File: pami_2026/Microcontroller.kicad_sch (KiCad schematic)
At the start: 1 part, among them U1 ESP32-WROOM-E

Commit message: WIP actuators
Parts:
- added C9: C, symbol Device:C
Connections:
- net +3.3V: now also C9.1; no longer U1.2 (3V3)
- net GND: now also U1.39 (GND_THERMAL)
- net SW_Team: now reaches U1.10 (DAC_1/ADC2_CH8/GPIO25)
- net SERVO_1: now reaches U1.11 (DAC_2/ADC2_CH9/GPIO26)
- net SERVO_2: now reaches U1.12 (ADC2_CH7/GPIO27)
- net PWM_B: now reaches U1.27 (GPIO16)
- net DC_A1: now reaches U1.28 (GPIO17)
- net PWM_A: now reaches U1.29 (GPIO5)
- net DC_A2: now reaches U1.30 (GPIO18)
- net DC_B1: now reaches U1.31 (GPIO19)
- net DC_B2: now reaches U1.33 (GPIO21)
- net TEAM_RGB: now reaches U1.36 (GPIO22)
- net SW_Tirette: now reaches U1.37 (GPIO23)
- new net: C9.2, U1.2 (3V3)

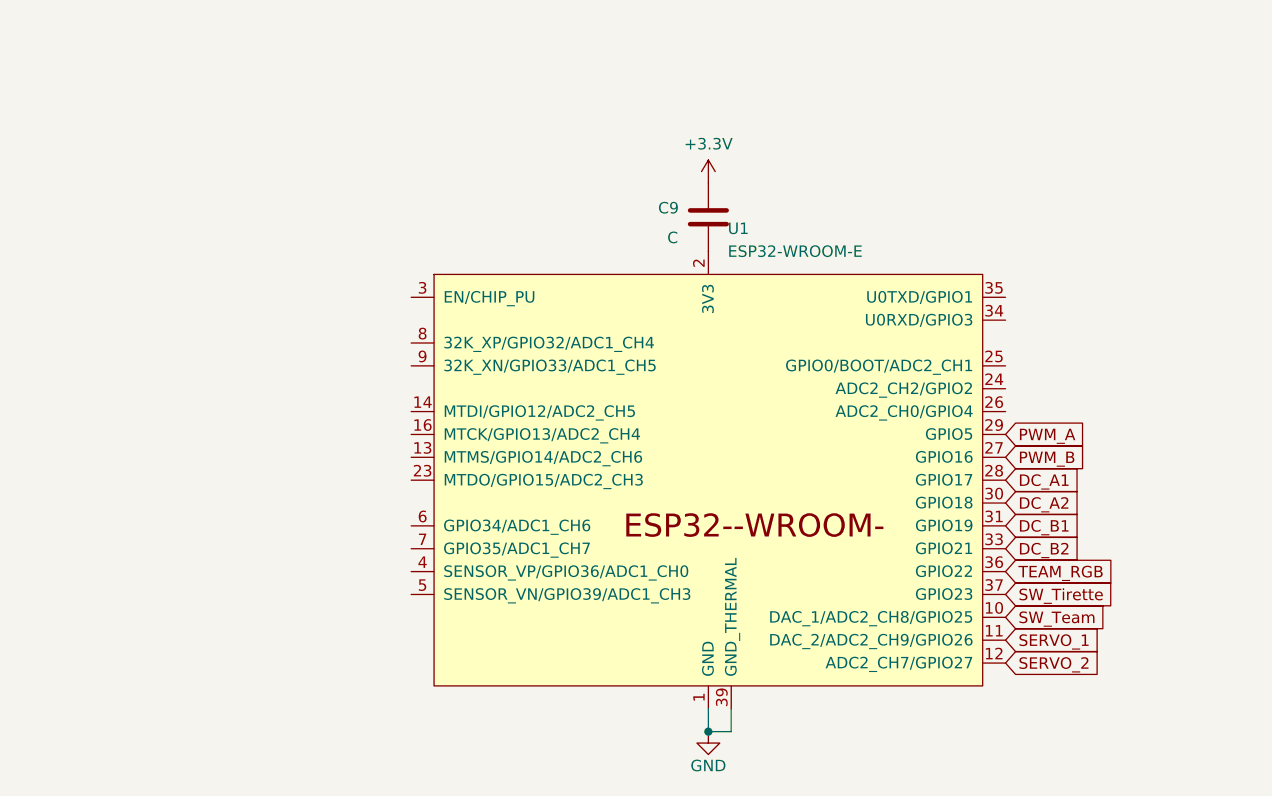
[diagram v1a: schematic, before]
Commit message: WIP USB programmer
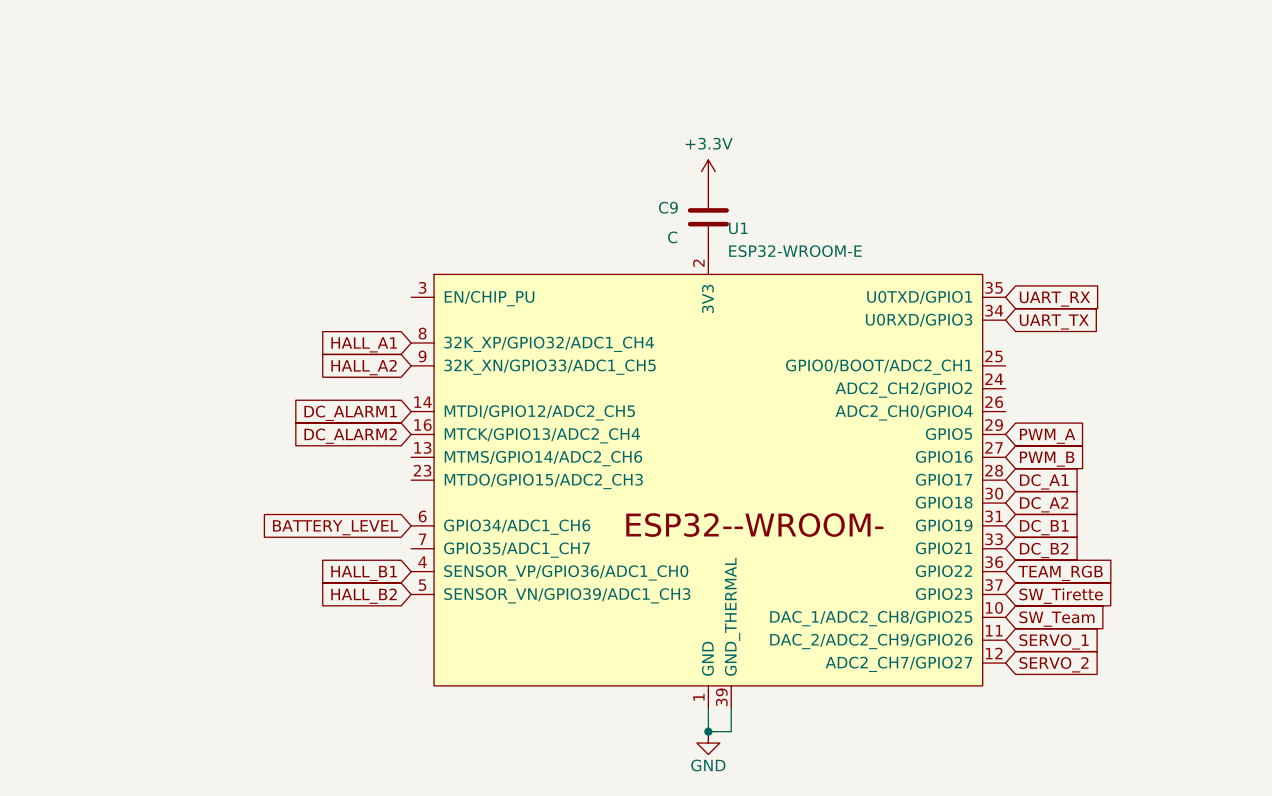
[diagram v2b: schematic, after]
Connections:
- net DC_ALARM1: now reaches U1.14 (MTDI/GPIO12/ADC2_CH5)
- net DC_ALARM2: now reaches U1.16 (MTCK/GPIO13/ADC2_CH4)
- net UART_TX: now reaches U1.34 (U0RXD/GPIO3)
- net UART_RX: now reaches U1.35 (U0TXD/GPIO1)
- net HALL_B1: now reaches U1.4 (SENSOR_VP/GPIO36/ADC1_CH0)
- net HALL_B2: now reaches U1.5 (SENSOR_VN/GPIO39/ADC1_CH3)
- net BATTERY_LEVEL: now reaches U1.6 (GPIO34/ADC1_CH6)
- net HALL_A1: now reaches U1.8 (32K_XP/GPIO32/ADC1_CH4)
- net HALL_A2: now reaches U1.9 (32K_XN/GPIO33/ADC1_CH5)
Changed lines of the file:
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@@
+		)
+	)
+	(global_label "UART_RX"
+		(shape input)
+		(at 176.53 63.5 0)
+		(fields_autoplaced yes)
+		(effects
+			(font
+				(size 1.27 1.27)
+			)
+			(justify left)
+		)
+		(property "Intersheetrefs" "${INTERSHEET_REFS}"
+			(at 187.619 63.5 0)
+			(effects
+				(font
+					(size 1.27 1.27)
+				)
+				(justify left)
+				(hide yes)
+			)
 		)
 	)
@@
 		)
 	)
+	(global_label "HALL_A2"
+		(shape input)
+		(at 110.49 71.12 180)
+		(fields_autoplaced yes)
+		(effects
+			(font
+				(size 1.27 1.27)
+			)
+			(justify right)
+		)
+		(property "Intersheetrefs" "${INTERSHEET_REFS}"
+			(at 99.7638 71.12 0)
+			(effects
+				(font
+					(size 1.27 1.27)
+				)
+				(justify right)
+				(hide yes)
+			)
+		)
+	)
 	(global_label "SW_Team"
 		(shape input)
@@
 		)
 	)
+	(global_label "BATTERY_LEVEL"
+		(shape input)
+		(at 110.49 88.9 180)
+		(fields_autoplaced yes)
+		(effects
+			(font
+				(size 1.27 1.27)
+			)
+			(justify right)
+		)
+		(property "Intersheetrefs" "${INTERSHEET_REFS}"
+			(at 93.293 88.9 0)
+			(effects
+				(font
+					(size 1.27 1.27)
+				)
+				(justify right)
+				(hide yes)
+			)
+		)
+	)
+	(global_label "DC_ALARM1"
+		(shape input)
+		(at 110.49 76.2 180)
+		(fields_autoplaced yes)
+		(effects
+			(font
+				(size 1.27 1.27)
+			)
+			(justify right)
+		)
+		(property "Intersheetrefs" "${INTERSHEET_REFS}"
+			(at 96.861 76.2 0)
+			(effects
+				(font
+					(size 1.27 1.27)
+				)
+				(justify right)
+				(hide yes)
+			)
+		)
+	)
 	(global_label "PWM_B"
 		(shape input)
@@
 		)
 	)
+	(global_label "HALL_B2"
+		(shape input)
+		(at 110.49 96.52 180)
+		(fields_autoplaced yes)
+		(effects
+			(font
+				(size 1.27 1.27)
+			)
+			(justify right)
+		)
+		(property "Intersheetrefs" "${INTERSHEET_REFS}"
+			(at 99.5824 96.52 0)
+			(effects
+				(font
+					(size 1.27 1.27)
+				)
+				(justify right)
+				(hide yes)
+			)
+		)
+	)
 	(global_label "PWM_A"
 		(shape input)
@@
 		)
 	)
+	(global_label "UART_TX"
+		(shape input)
+		(at 176.53 66.04 0)
+		(fields_autoplaced yes)
+		(effects
+			(font
+				(size 1.27 1.27)
+			)
+			(justify left)
+		)
+		(property "Intersheetrefs" "${INTERSHEET_REFS}"
+			(at 187.3166 66.04 0)
+			(effects
+				(font
+					(size 1.27 1.27)
+				)
+				(justify left)
+				(hide yes)
+			)
+		)
+	)
+	(global_label "HALL_A1"
+		(shape input)
+		(at 110.49 68.58 180)
+		(fields_autoplaced yes)
+		(effects
+			(font
+				(size 1.27 1.27)
+			)
+			(justify right)
+		)
+		(property "Intersheetrefs" "${INTERSHEET_REFS}"
+			(at 99.7638 68.58 0)
+			(effects
+				(font
+					(size 1.27 1.27)
+				)
+				(justify right)
+				(hide yes)
+			)
+		)
+	)
 	(global_label "SW_Tirette"
 		(shape input)
@@
 				(hide yes)
 			)
+		)
+	)
+	(global_label "DC_ALARM2"
+		(shape input)
+		(at 110.49 78.74 180)
+		(fields_autoplaced yes)
+		(effects
+			(font
+				(size 1.27 1.27)
+			)
+			(justify right)
+		)
+		(property "Intersheetrefs" "${INTERSHEET_REFS}"
+			(at 96.861 78.74 0)
+			(effects
+				(font
+					(size 1.27 1.27)
+				)
+				(justify right)
+				(hide yes)
+			)
+		)
+	)
+	(global_label "HALL_B1"
+		(shape input)
+		(at 110.49 93.98 180)
+		(fields_autoplaced yes)
+		(effects
+			(font
+				(size 1.27 1.27)
+			)
+			(justify right)
+		)
+		(property "Intersheetrefs" "${INTERSHEET_REFS}"
+			(at 99.5824 93.98 0)
+			(effects
+				(font
+					(size 1.27 1.27)
+				)
+				(justify right)
+				(hide yes)
+			)

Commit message: Change DC drivers, apply datasheet recommendations, add big capacitor, remove USB programmer for simple connector
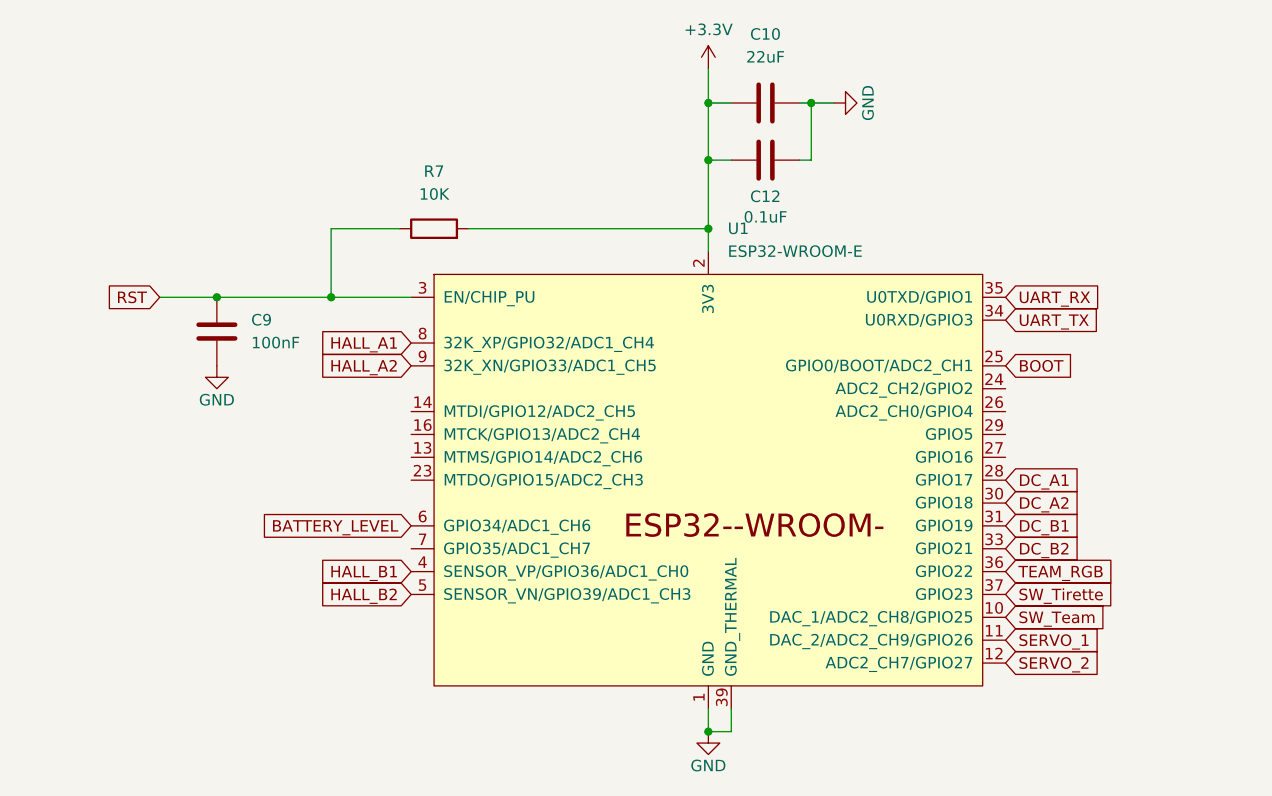
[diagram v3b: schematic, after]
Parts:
- added C10: 22uF, symbol Device:C
- added C12: 0.1uF, symbol Device:C
- added R7: 10K, symbol Device:R
- C9: value C -> 100nF
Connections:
- net +3.3V: now also U1.2 (3V3), C10.1, C12.1, R7.2; no longer C9.1
- net GND: now also C9.2, C10.2, C12.2
- net BOOT: now reaches U1.25 (GPIO0/BOOT/ADC2_CH1)
- net RST: now reaches U1.3 (EN/CHIP_PU)
- net RST: now also C9.1, R7.1
- net DC_ALARM1: no longer names the net of U1.14 (MTDI/GPIO12/ADC2_CH5)
- net DC_ALARM2: no longer names the net of U1.16 (MTCK/GPIO13/ADC2_CH4)
- net PWM_A: no longer names the net of U1.29 (GPIO5)
- net PWM_B: no longer names the net of U1.27 (GPIO16)

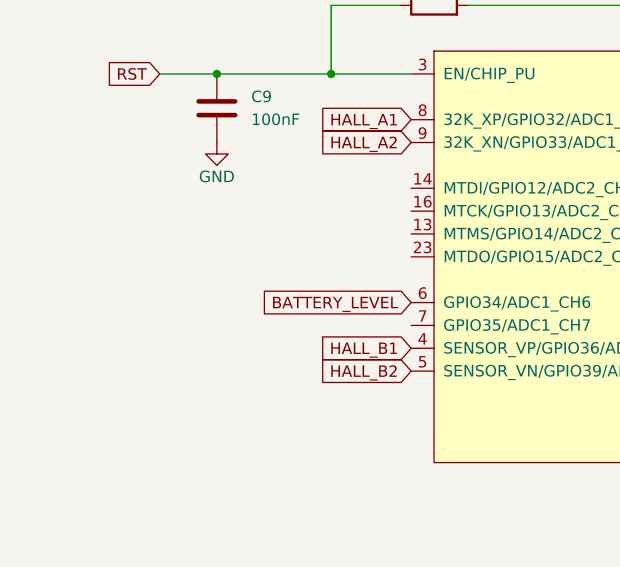
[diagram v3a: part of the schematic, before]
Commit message: Hall pull up
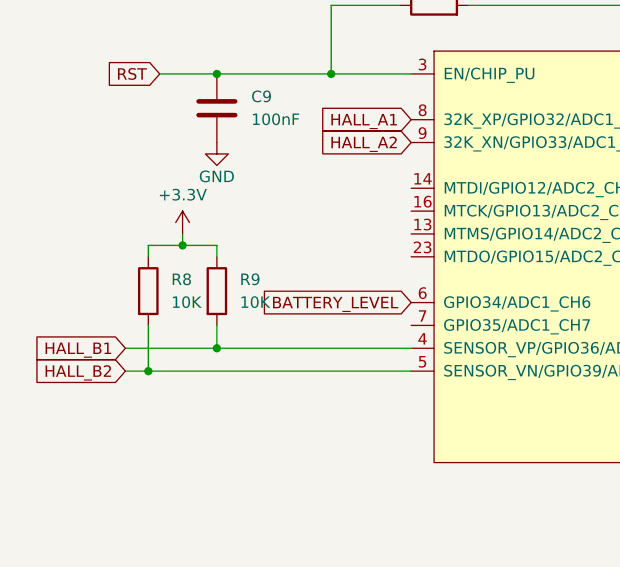
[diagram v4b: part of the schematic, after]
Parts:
- added R8, R9: 10K, symbol Device:R
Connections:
- net +3.3V: now also R8.1, R9.1
- net HALL_B1: now also R9.2
- net HALL_B2: now also R8.2

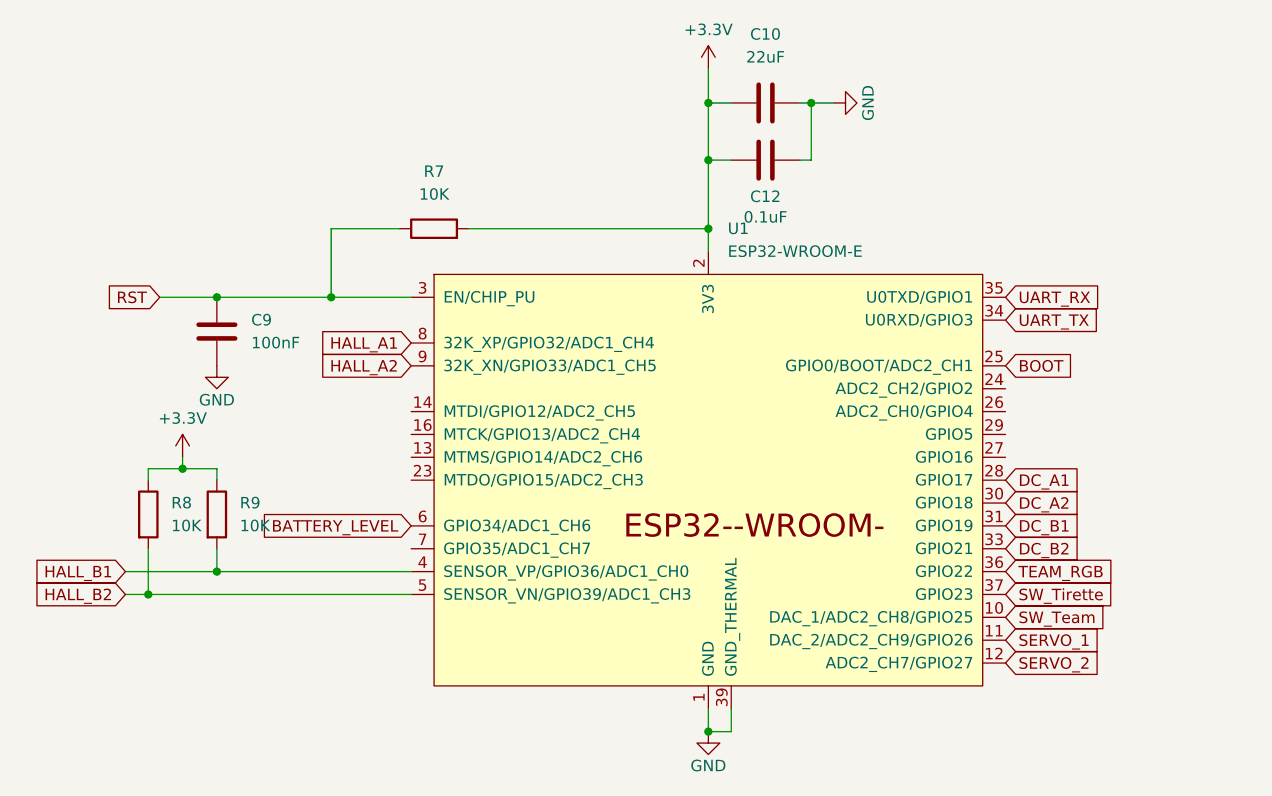
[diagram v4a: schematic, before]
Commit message: Ultrason, empreintes et petites corrections
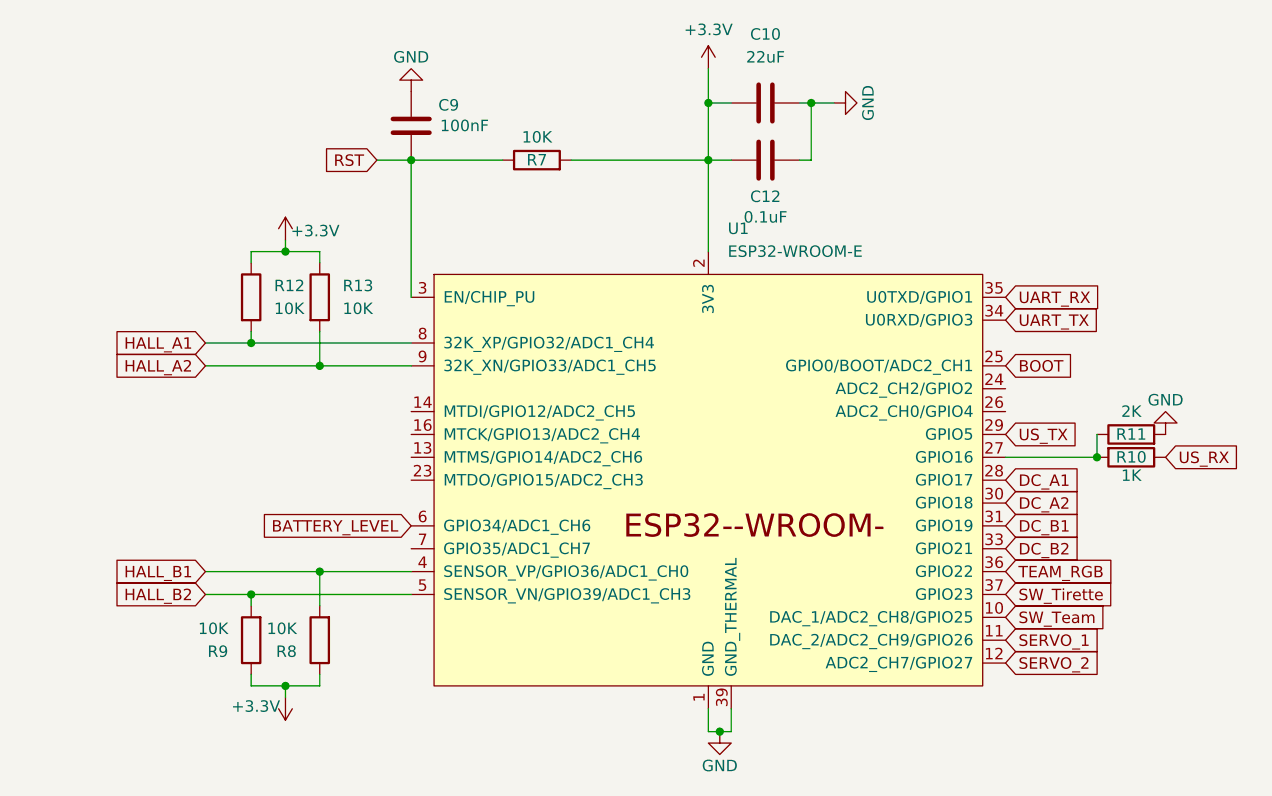
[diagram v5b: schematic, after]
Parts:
- added R10: 1K, Resistor_SMD:R_0603_1608Metric, symbol Device:R
- added R11: 2K, Resistor_SMD:R_0603_1608Metric, symbol Device:R
- added R12, R13: 10K, Resistor_SMD:R_0603_1608Metric, symbol Device:R
- C10: footprint (none) -> Capacitor_SMD:C_0805_2012Metric
- C12, C9: footprint (none) -> Capacitor_SMD:C_0603_1608Metric
- R7, R8, R9: footprint (none) -> Resistor_SMD:R_0603_1608Metric
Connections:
- net +3.3V: now also R12.1, R13.1
- net GND: now also R11.2
- net HALL_A1: now also R12.2
- net HALL_A2: now also R13.2
- net HALL_B1: now also R8.2; no longer R9.2
- net HALL_B2: now also R9.2; no longer R8.2
- net at U1.27 (GPIO16): now also R10.2, R11.1
- net US_TX: now reaches U1.29 (GPIO5)
- new net US_RX: R10.1
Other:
- moved on the sheet: C9, R7, R8, R9
